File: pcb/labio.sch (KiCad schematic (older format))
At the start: 0 parts

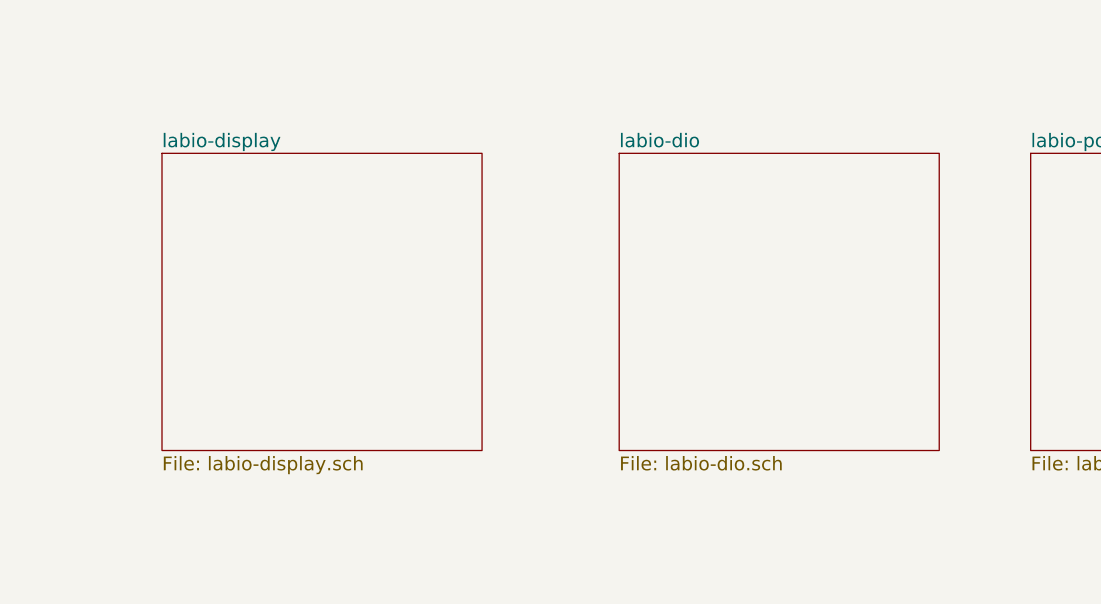
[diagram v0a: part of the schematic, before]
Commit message: add schematics for display and dio (dpad, servo, motor, encoder)
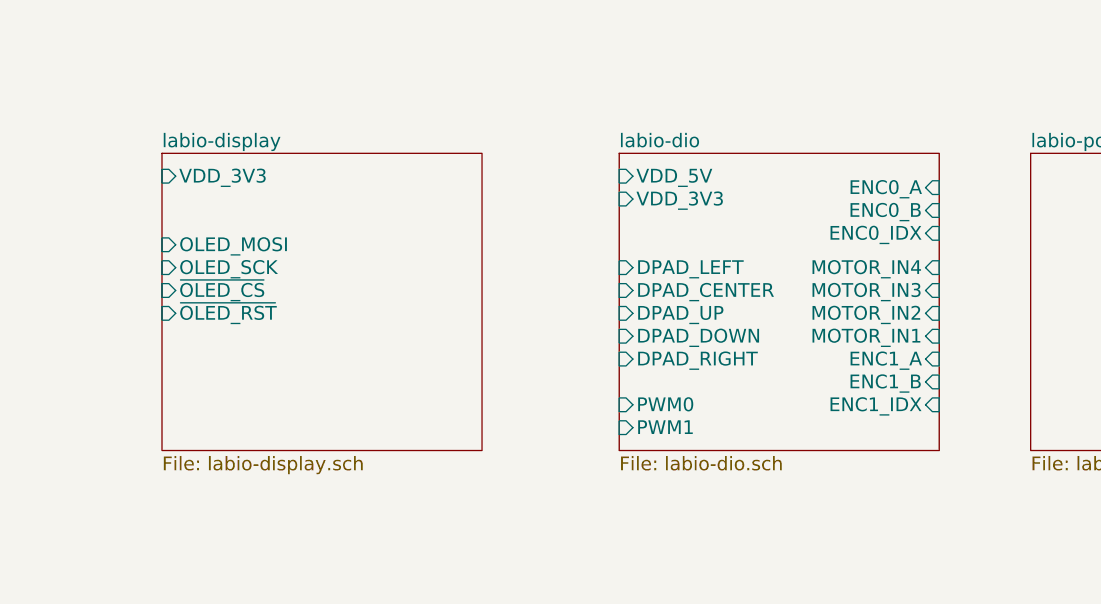
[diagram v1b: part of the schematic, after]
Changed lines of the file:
@@
 $Descr A4 11693 8268
 encoding utf-8
-Sheet 1 7
+Sheet 1 8
 Title ""
 Date ""
@@
 F0 "labio-display" 60
 F1 "labio-display.sch" 60
+F2 "VDD_3V3" I L 3700 3200 60
+F3 "~OLED_CS" I L 3700 3700 60
+F4 "~OLED_RST" I L 3700 3800 60
+F5 "OLED_SCK" I L 3700 3600 60
+F6 "OLED_MOSI" I L 3700 3500 60
 $EndSheet
 $Sheet
@@
 F0 "labio-dio" 60
 F1 "labio-dio.sch" 60
+F2 "DPAD_LEFT" I L 5700 3600 60
+F3 "DPAD_CENTER" I L 5700 3700 60
+F4 "DPAD_UP" I L 5700 3800 60
+F5 "DPAD_DOWN" I L 5700 3900 60
+F6 "DPAD_RIGHT" I L 5700 4000 60
+F7 "VDD_3V3" I L 5700 3300 60
+F8 "PWM0" I L 5700 4200 60
+F9 "PWM1" I L 5700 4300 60
+F10 "MOTOR_IN4" I R 7100 3600 60
+F11 "MOTOR_IN2" I R 7100 3800 60
+F12 "MOTOR_IN3" I R 7100 3700 60
+F13 "MOTOR_IN1" I R 7100 3900 60
+F14 "VDD_5V" I L 5700 3200 60
+F15 "ENC1_A" I R 7100 4000 60
+F16 "ENC1_B" I R 7100 4100 60
+F17 "ENC1_IDX" I R 7100 4200 60
+F18 "ENC0_A" I R 7100 3250 60
+F19 "ENC0_B" I R 7100 3350 60
+F20 "ENC0_IDX" I R 7100 3450 60
 $EndSheet
 $Sheet

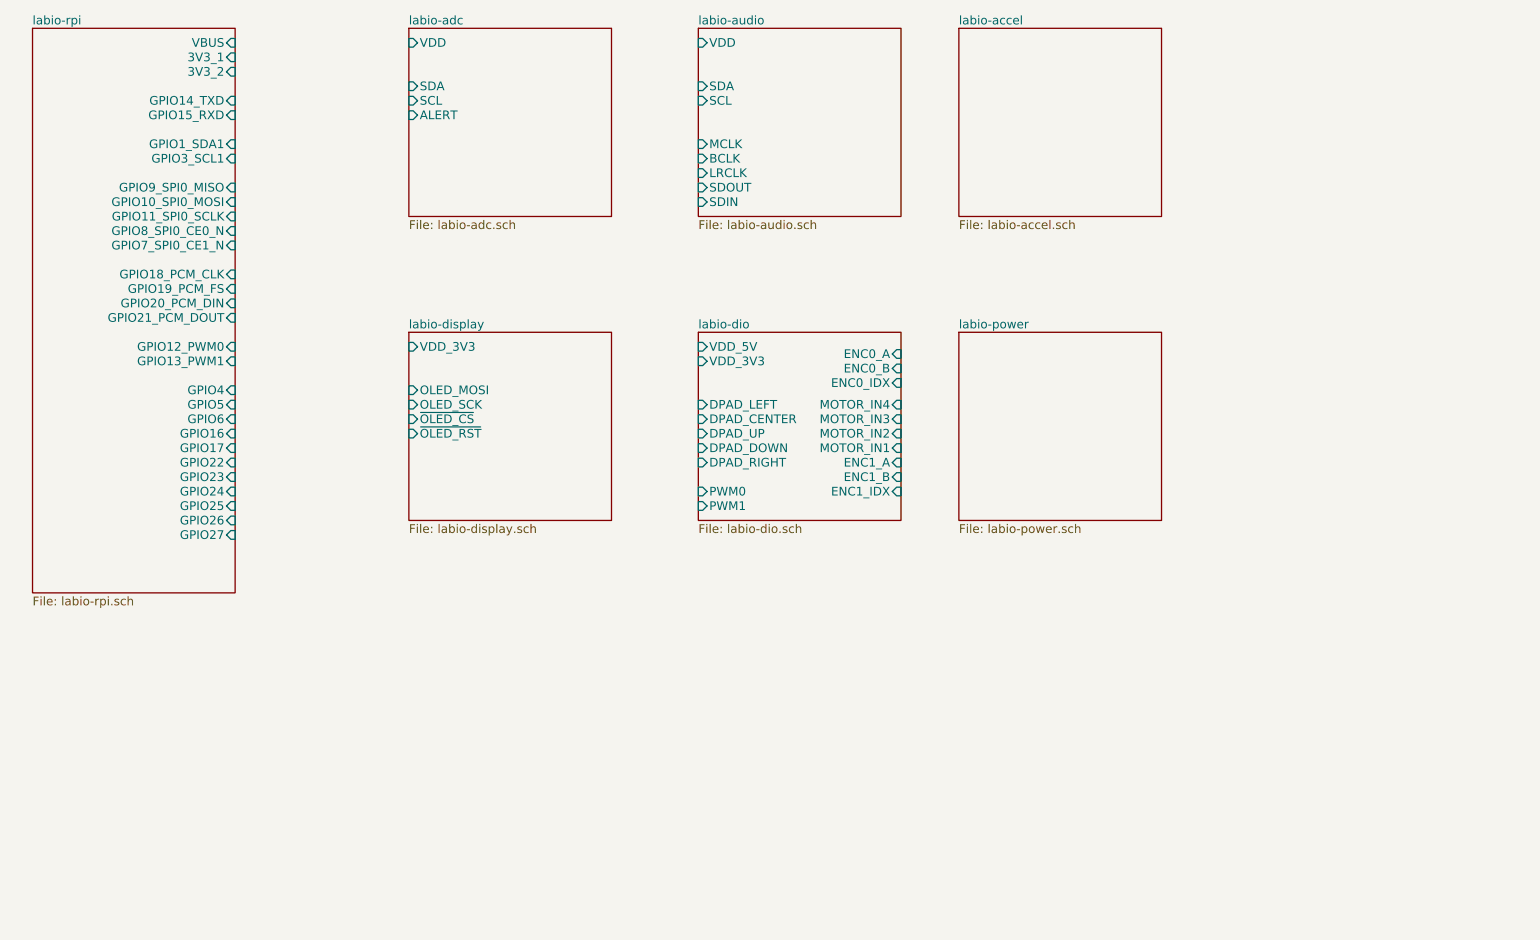
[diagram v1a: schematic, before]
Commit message: add imu sensors, make top level connections
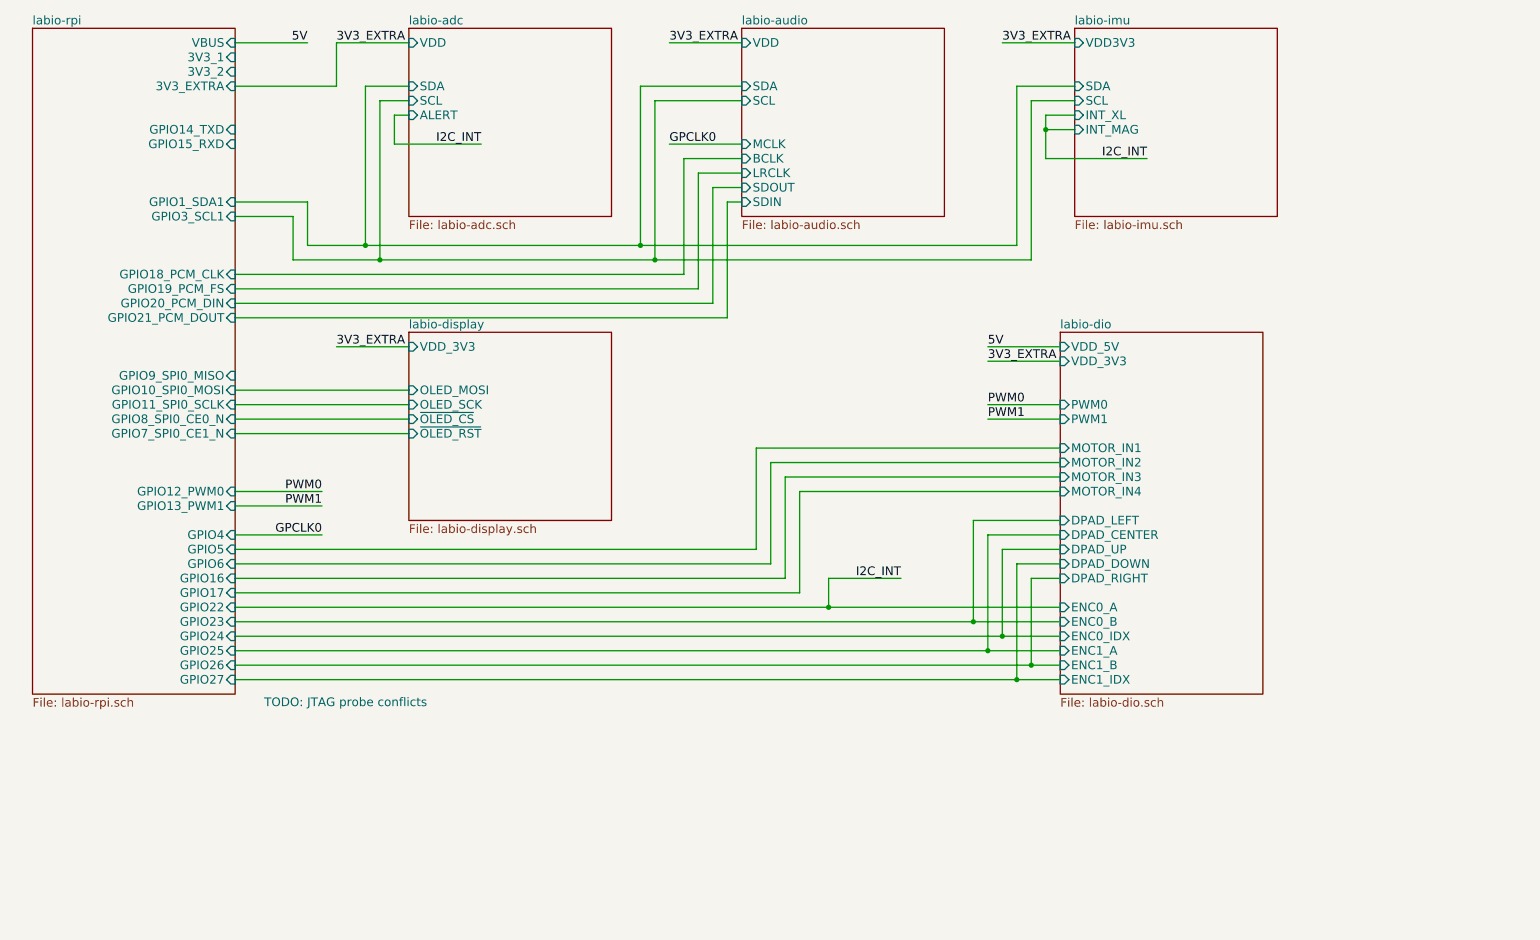
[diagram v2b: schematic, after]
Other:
- note added: "TODO: JTAG probe conflicts"

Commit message: finish rpi to module connections
* use dip switches to disable/configure blocks
* add light sensor
* fix motor controller sense resistors
* fix overused jtag probe pins
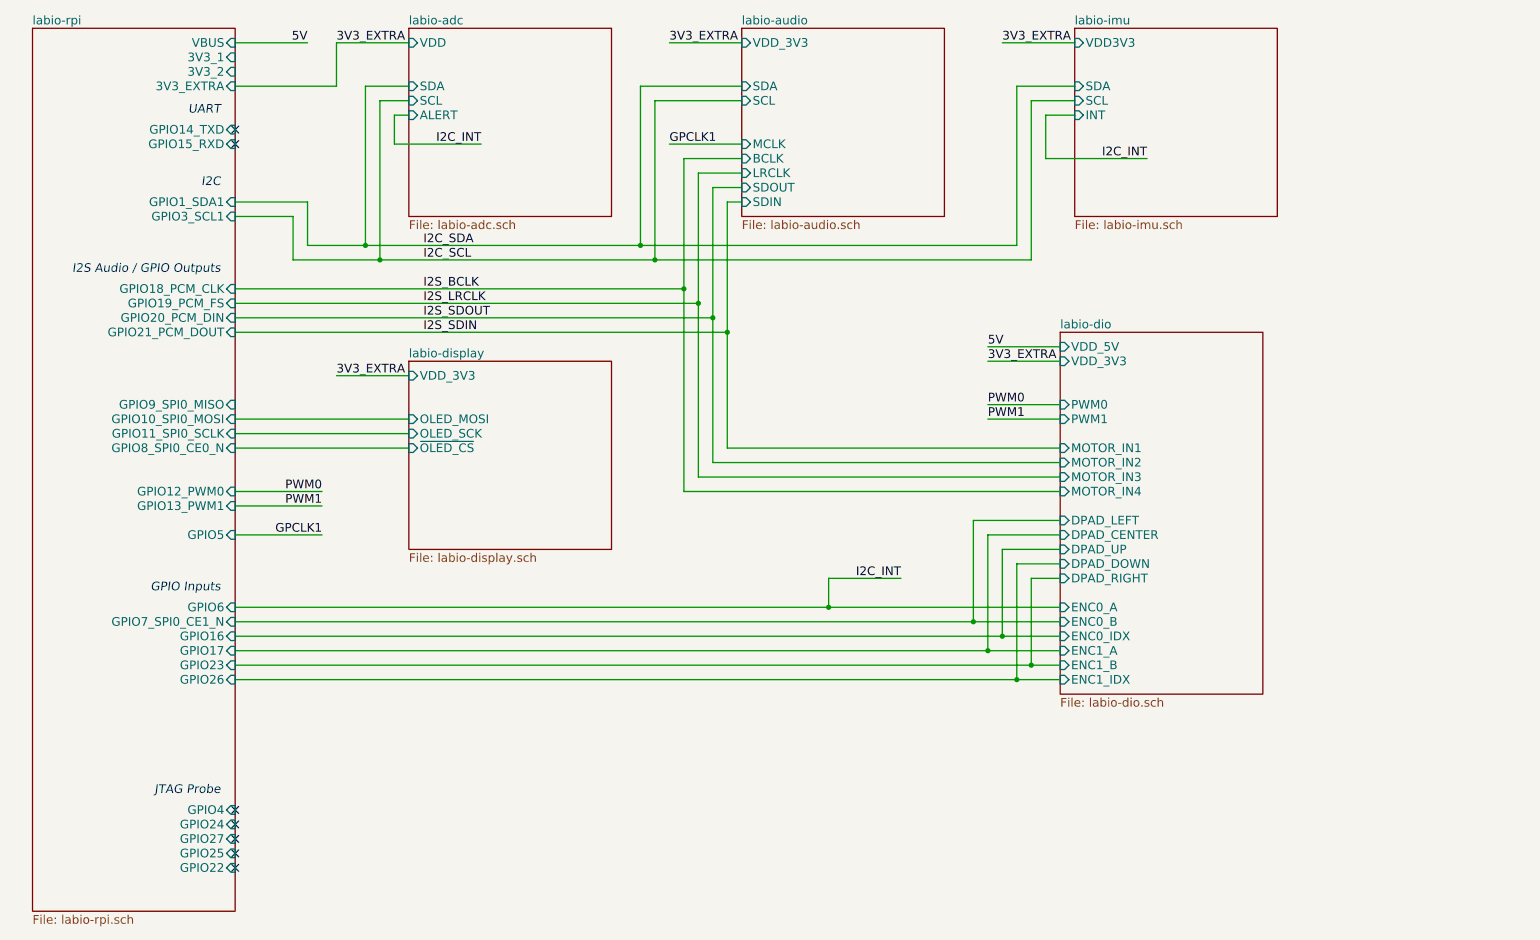
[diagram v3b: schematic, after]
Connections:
- no-connect marks 0 -> 7
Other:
- note added: "GPIO Inputs"
- note added: "I2C"
- note added: "I2S Audio / GPIO Outputs"
- note added: "JTAG Probe"
- note added: "UART"
- note removed: "TODO: JTAG probe conflicts"
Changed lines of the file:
@@
 $EndDescr
 $Sheet
-S 1100 1000 1400 4600
+S 1100 1000 1400 6100
 U 572692EE
 F0 "labio-rpi" 60
 F1 "labio-rpi.sch" 60
 F2 "3V3_1" I R 2500 1200 60
-F3 "GPIO4" I R 2500 4500 60
-F4 "GPIO27" I R 2500 5500 60
-F5 "GPIO22" I R 2500 5000 60
-F6 "GPIO10_SPI0_MOSI" I R 2500 3500 60
-F7 "GPIO9_SPI0_MISO" I R 2500 3400 60
+F3 "GPIO4" I R 2500 6400 60
+F4 "GPIO27" I R 2500 6600 60
+F5 "GPIO22" I R 2500 6800 60
+F6 "GPIO10_SPI0_MOSI" I R 2500 3700 60
+F7 "GPIO9_SPI0_MISO" I R 2500 3600 60
 F8 "3V3_2" I R 2500 1300 60
-F9 "GPIO11_SPI0_SCLK" I R 2500 3600 60
-F10 "GPIO5" I R 2500 4600 60
-F11 "GPIO6" I R 2500 4700 60
-F12 "GPIO26" I R 2500 5400 60
+F9 "GPIO11_SPI0_SCLK" I R 2500 3800 60
+F10 "GPIO5" I R 2500 4500 60
+F11 "GPIO6" I R 2500 5000 60
+F12 "GPIO26" I R 2500 5500 60
 F13 "VBUS" I R 2500 1100 60
 F14 "GPIO14_TXD" I R 2500 1700 60
 F15 "GPIO15_RXD" I R 2500 1800 60
-F16 "GPIO23" I R 2500 5100 60
-F17 "GPIO24" I R 2500 5200 60
-F18 "GPIO25" I R 2500 5300 60
-F19 "GPIO8_SPI0_CE0_N" I R 2500 3700 60
-F20 "GPIO7_SPI0_CE1_N" I R 2500 3800 60
+F16 "GPIO23" I R 2500 5400 60
+F17 "GPIO24" I R 2500 6500 60
+F18 "GPIO25" I R 2500 6700 60
+F19 "GPIO8_SPI0_CE0_N" I R 2500 3900 60
+F20 "GPIO7_SPI0_CE1_N" I R 2500 5100 60
 F21 "GPIO1_SDA1" I R 2500 2200 60
 F22 "GPIO3_SCL1" I R 2500 2300 60
-F23 "GPIO17" I R 2500 4900 60
+F23 "GPIO17" I R 2500 5300 60
 F24 "GPIO13_PWM1" I R 2500 4300 60
-F25 "GPIO19_PCM_FS" I R 2500 2800 60
-F26 "GPIO18_PCM_CLK" I R 2500 2700 60
+F25 "GPIO19_PCM_FS" I R 2500 2900 60
+F26 "GPIO18_PCM_CLK" I R 2500 2800 60
 F27 "GPIO12_PWM0" I R 2500 4200 60
-F28 "GPIO16" I R 2500 4800 60
-F29 "GPIO20_PCM_DIN" I R 2500 2900 60
-F30 "GPIO21_PCM_DOUT" I R 2500 3000 60
+F28 "GPIO16" I R 2500 5200 60
+F29 "GPIO20_PCM_DIN" I R 2500 3000 60
+F30 "GPIO21_PCM_DOUT" I R 2500 3100 60
 F31 "3V3_EXTRA" I R 2500 1400 60
 $EndSheet
@@
 $EndSheet
 $Sheet
-S 6000 1000 1400 1300
-U 57483D93
-F0 "labio-audio" 60
-F1 "labio-audio.sch" 60
-F2 "VDD" I L 6000 1100 60
-F3 "SDA" I L 6000 1400 60
-F4 "SCL" I L 6000 1500 60
-F5 "MCLK" I L 6000 1800 60
-F6 "BCLK" I L 6000 1900 60
-F7 "LRCLK" I L 6000 2000 60
-F8 "SDIN" I L 6000 2200 60
-F9 "SDOUT" I L 6000 2100 60
-$EndSheet
-$Sheet
-S 3700 3100 1400 1300
+S 3700 3300 1400 1300
 U 57483FA2
 F0 "labio-display" 60
 F1 "labio-display.sch" 60
-F2 "VDD_3V3" I L 3700 3200 60
-F3 "~OLED_CS" I L 3700 3700 60
-F4 "~OLED_RST" I L 3700 3800 60
-F5 "OLED_SCK" I L 3700 3600 60
-F6 "OLED_MOSI" I L 3700 3500 60
+F2 "VDD_3V3" I L 3700 3400 60
+F3 "~OLED_CS" I L 3700 3900 60
+F4 "OLED_SCK" I L 3700 3800 60
+F5 "OLED_MOSI" I L 3700 3700 60
 $EndSheet
 $Sheet
@@
 F1 "labio-imu.sch" 60
 F2 "VDD3V3" I L 8300 1100 60
-F3 "INT_XL" I L 8300 1600 60
-F4 "INT_MAG" I L 8300 1700 60
-F5 "SCL" I L 8300 1500 60
-F6 "SDA" I L 8300 1400 60
+F3 "SCL" I L 8300 1500 60
+F4 "SDA" I L 8300 1400 60
+F5 "INT" I L 8300 1600 60
 $EndSheet
 $Sheet
@@
 Connection ~ 5400 2600
 Wire Wire Line
-	2500 2700 5600 2700
-Wire Wire Line
-	5600 2700 5600 1900
+	2500 2800 5600 2800
+Wire Wire Line
+	5600 1900 5600 4200
 Wire Wire Line
 	5600 1900 6000 1900
 Wire Wire Line
-	2500 2800 5700 2800
-Wire Wire Line
-	5700 2800 5700 2000
+	2500 2900 5700 2900
+Wire Wire Line
+	5700 2000 5700 4100
 Wire Wire Line
 	5700 2000 6000 2000
 Wire Wire Line
-	2500 2900 5800 2900
-Wire Wire Line
-	5800 2900 5800 2100
+	2500 3000 5800 3000
+Wire Wire Line
+	5800 2100 5800 4000
 Wire Wire Line
 	5800 2100 6000 2100
 Wire Wire Line
-	2500 3000 5900 3000
-Wire Wire Line
-	5900 3000 5900 2200
+	2500 3100 5900 3100
+Wire Wire Line
+	5900 2200 5900 3900
 Wire Wire Line
 	5900 2200 6000 2200
@@
 	5500 1800 6000 1800
 Wire Wire Line
-	8200 3900 6100 3900
-Wire Wire Line
-	6100 3900 6100 4600
-Wire Wire Line
-	6100 4600 2500 4600
-Wire Wire Line
-	2500 4700 6200 4700
-Wire Wire Line
-	6200 4700 6200 4000
-Wire Wire Line
-	6200 4000 8200 4000
-Wire Wire Line
-	2500 4900 6400 4900
-Wire Wire Line
-	6400 4900 6400 4200
-Wire Wire Line
-	6400 4200 8200 4200
-Wire Wire Line
-	8200 4100 6300 4100
-Wire Wire Line
-	6300 4100 6300 4800
-Wire Wire Line
-	6300 4800 2500 4800
-Wire Wire Line
-	3200 3200 3700 3200
-Wire Wire Line
-	3700 3500 2500 3500
-Wire Wire Line
-	2500 3700 3700 3700
-Wire Wire Line
-	3700 3600 2500 3600
-Wire Wire Line
-	2500 3800 3700 3800
+	3200 3400 3700 3400
+Wire Wire Line
+	3700 3700 2500 3700
+Wire Wire Line
+	2500 3900 3700 3900
+Wire Wire Line
+	3700 3800 2500 3800
 Wire Wire Line
 	8200 4700 7900 4700
@@
 Wire Wire Line
 	8300 1600 8100 1600
-Wire Wire Line
-	8100 1700 8300 1700
-Connection ~ 8100 1700
 Wire Wire Line
 	7700 3300 8200 3300
@@
 5V
 Text Label 5500 1800 0    60   ~ 0
-GPCLK0
+GPCLK1
 Wire Wire Line
 	2500 4500 3100 4500
 Text Label 3100 4500 2    60   ~ 0
-GPCLK0
-Text Label 3200 3200 0    60   ~ 0
+GPCLK1
+Text Label 3200 3400 0    60   ~ 0
 3V3_EXTRA
 Wire Wire Line
@@
 Text Label 4200 1800 2    60   ~ 0
 I2C_INT
-Text Notes 2700 5700 0    60   ~ 0
-TODO: JTAG probe conflicts
+Text Notes 2400 6300 2    60   Italic 0
+JTAG Probe
+Text Label 3800 2500 0    60   ~ 0
+I2C_SDA
+Text Label 3800 2600 0    60   ~ 0
+I2C_SCL
+Text Label 3800 2800 0    60   ~ 0
+I2S_BCLK
+Text Label 3800 2900 0    60   ~ 0
+I2S_LRCLK
+Text Label 3800 3000 0    60   ~ 0
+I2S_SDOUT
+Text Label 3800 3100 0    60   ~ 0
+I2S_SDIN
+Wire Wire Line
+	5900 3900 8200 3900
+Connection ~ 5900 3100
+Wire Wire Line
+	5800 4000 8200 4000
+Connection ~ 5800 3000
+Wire Wire Line
+	5700 4100 8200 4100
+Connection ~ 5700 2900
+Wire Wire Line
+	5600 4200 8200 4200
+Connection ~ 5600 2800
+Text Notes 2400 4900 2    60   Italic 0
+GPIO Inputs
+Text Notes 2400 2700 2    60   Italic 0
+I2S Audio / GPIO Outputs
+Text Notes 2400 2100 2    60   Italic 0
+I2C
+Text Notes 2400 1600 2    60   Italic 0
+UART
+$Sheet
+S 6000 1000 1400 1300
+U 57483D93
+F0 "labio-audio" 60
+F1 "labio-audio.sch" 60
+F2 "SDA" I L 6000 1400 60
+F3 "SCL" I L 6000 1500 60
+F4 "MCLK" I L 6000 1800 60
+F5 "BCLK" I L 6000 1900 60
+F6 "LRCLK" I L 6000 2000 60
+F7 "SDIN" I L 6000 2200 60
+F8 "SDOUT" I L 6000 2100 60
+F9 "VDD_3V3" I L 6000 1100 60
+$EndSheet
+NoConn ~ 2500 6800
+NoConn ~ 2500 6700
+NoConn ~ 2500 6600
+NoConn ~ 2500 6500
+NoConn ~ 2500 6400
+NoConn ~ 2500 1800
+NoConn ~ 2500 1700
 $EndSCHEMATC
